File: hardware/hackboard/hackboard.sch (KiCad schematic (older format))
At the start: 22 parts, among them J1 Power, J2 Lil Cup, J3 Chonk Cup, J4 JTAG, Q1 Mosfet, Q2 Mosfet, U1 AP63200, U2 ESP32-WROVER-E

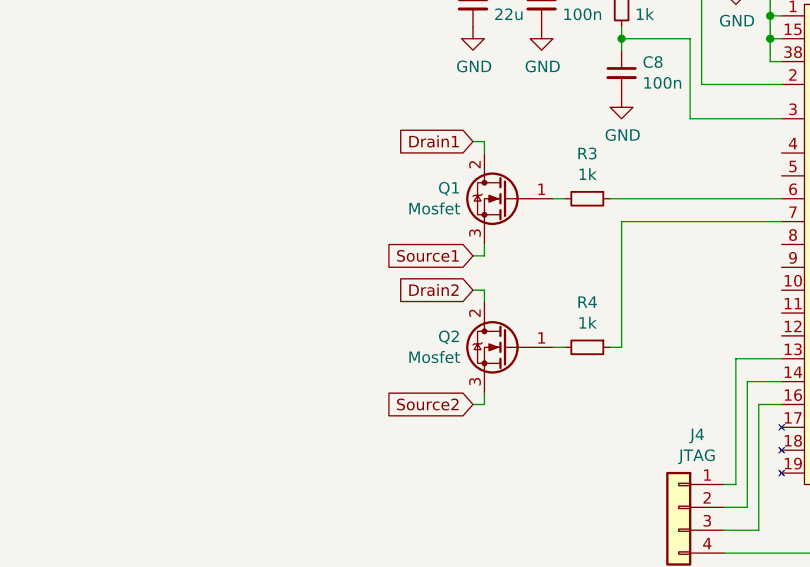
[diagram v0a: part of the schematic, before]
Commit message: Footprints zugewiesen, Bauteile angefangen zu plazieren
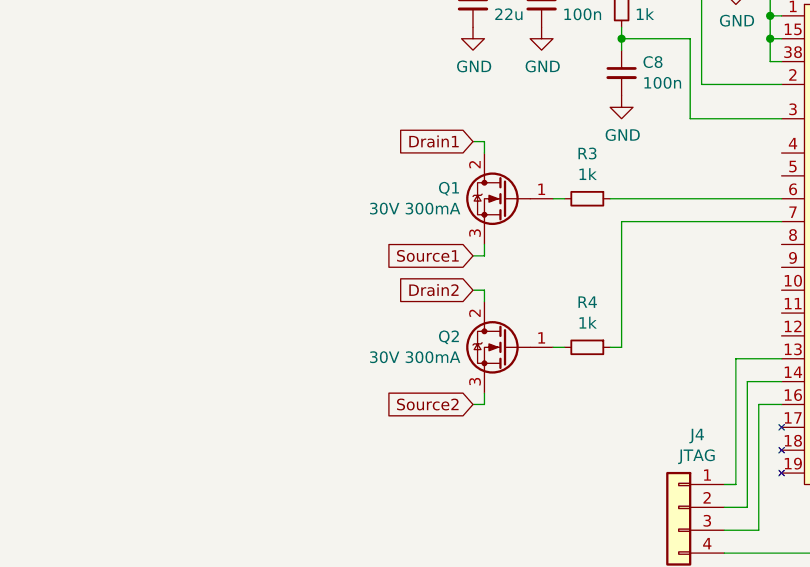
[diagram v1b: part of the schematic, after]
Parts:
- C1, C4, C5, C6: footprint (none) -> Capacitor_SMD:C_1210_3225Metric_Pad1.42x2.65mm_HandSolder
- C2, C3, C7, C8: footprint (none) -> Capacitor_SMD:C_0603_1608Metric_Pad1.05x0.95mm_HandSolder
- J1: footprint (none) -> Connector_Molex:Molex_KK-254_AE-6410-02A_1x02_P2.54mm_Vertical
- J2, J3: footprint (none) -> Connector_Molex:Molex_KK-254_AE-6410-03A_1x03_P2.54mm_Vertical
- J4: footprint (none) -> Connector_Molex:Molex_KK-254_AE-6410-06A_1x06_P2.54mm_Vertical
- L1: footprint (none) -> n-level:WE-7345
- Q1, Q2: value Mosfet -> 30V 300mA; footprint (none) -> Package_TO_SOT_SMD:SOT-23_Handsoldering
- R1, R2, R3, R4, R5: footprint (none) -> Resistor_SMD:R_0603_1608Metric_Pad1.05x0.95mm_HandSolder
- U1: footprint (none) -> Package_TO_SOT_SMD:TSOT-23-6_HandSoldering
- U2: footprint (none) -> n-level:ESP32-WROOM-ROVER
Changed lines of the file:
@@
 F 0 "U2" H 6750 2377 50  0000 C CNN
 F 1 "ESP32-WROVER-E" H 6750 2286 50  0000 C CNN
-F 2 "" H 6750 3450 50  0001 C CNN
+F 2 "n-level:ESP32-WROOM-ROVER" H 6750 3450 50  0001 C CNN
 F 3 "" H 6750 3450 50  0001 C CNN
 	1    6750 3500
@@
 F 0 "J1" H 568 2867 50  0000 C CNN
 F 1 "Power" H 568 2776 50  0000 C CNN
-F 2 "" H 650 2650 50  0001 C CNN
+F 2 "Connector_Molex:Molex_KK-254_AE-6410-02A_1x02_P2.54mm_Vertical" H 650 2650 50  0001 C CNN
 F 3 "~" H 650 2650 50  0001 C CNN
 	1    650  2650
@@
 F 0 "R1" H 3259 6846 50  0000 L CNN
 F 1 "182k" H 3259 6755 50  0000 L CNN
-F 2 "" H 3200 6800 50  0001 C CNN
+F 2 "Resistor_SMD:R_0603_1608Metric_Pad1.05x0.95mm_HandSolder" H 3200 6800 50  0001 C CNN
 F 3 "~" H 3200 6800 50  0001 C CNN
 	1    3200 6800
@@
 P 4850 3300
 F 0 "Q1" H 5055 3346 50  0000 L CNN
-F 1 "Mosfet" H 5055 3255 50  0000 L CNN
-F 2 "" H 5050 3400 50  0001 C CNN
+F 1 "30V 300mA" H 5055 3255 50  0000 L CNN
+F 2 "Package_TO_SOT_SMD:SOT-23_Handsoldering" H 5050 3400 50  0001 C CNN
 F 3 "~" H 4850 3300 50  0001 C CNN
 	1    4850 3300
@@
 F 0 "C1" H 1292 6996 50  0000 L CNN
 F 1 "10u" H 1292 6905 50  0000 L CNN
-F 2 "" H 1200 6950 50  0001 C CNN
+F 2 "Capacitor_SMD:C_1210_3225Metric_Pad1.42x2.65mm_HandSolder" H 1200 6950 50  0001 C CNN
 F 3 "~" H 1200 6950 50  0001 C CNN
 	1    1200 6950
@@
 F 0 "U1" H 1850 7415 50  0000 C CNN
 F 1 "AP63200" H 1850 7324 50  0000 C CNN
-F 2 "" H 1850 7400 50  0001 C CNN
+F 2 "Package_TO_SOT_SMD:TSOT-23-6_HandSoldering" H 1850 7400 50  0001 C CNN
 F 3 "" H 1850 7400 50  0001 C CNN
 	1    1850 6950
@@
 F 0 "C2" V 2171 6650 50  0000 C CNN
 F 1 "100n" V 2262 6650 50  0000 C CNN
-F 2 "" H 2400 6650 50  0001 C CNN
+F 2 "Capacitor_SMD:C_0603_1608Metric_Pad1.05x0.95mm_HandSolder" H 2400 6650 50  0001 C CNN
 F 3 "~" H 2400 6650 50  0001 C CNN
 	1    2400 6650
@@
 F 0 "L1" V 2885 6650 50  0000 C CNN
 F 1 "10u" V 2794 6650 50  0000 C CNN
-F 2 "" H 2700 6650 50  0001 C CNN
+F 2 "n-level:WE-7345" H 2700 6650 50  0001 C CNN
 F 3 "~" H 2700 6650 50  0001 C CNN
 	1    2700 6650
@@
 F 0 "C3" H 2942 6846 50  0000 L CNN
 F 1 "100p" H 2942 6755 50  0000 L CNN
-F 2 "" H 2850 6800 50  0001 C CNN
+F 2 "Capacitor_SMD:C_0603_1608Metric_Pad1.05x0.95mm_HandSolder" H 2850 6800 50  0001 C CNN
 F 3 "~" H 2850 6800 50  0001 C CNN
 	1    2850 6800
@@
 F 0 "R2" H 3259 7146 50  0000 L CNN
 F 1 "62k" H 3259 7055 50  0000 L CNN
-F 2 "" H 3200 7100 50  0001 C CNN
+F 2 "Resistor_SMD:R_0603_1608Metric_Pad1.05x0.95mm_HandSolder" H 3200 7100 50  0001 C CNN
 F 3 "~" H 3200 7100 50  0001 C CNN
 	1    3200 7100
@@
 F 0 "C4" H 3642 6996 50  0000 L CNN
 F 1 "22u" H 3642 6905 50  0000 L CNN
-F 2 "" H 3550 6950 50  0001 C CNN
+F 2 "Capacitor_SMD:C_1210_3225Metric_Pad1.42x2.65mm_HandSolder" H 3550 6950 50  0001 C CNN
 F 3 "~" H 3550 6950 50  0001 C CNN
 	1    3550 6950
@@
 F 0 "C5" H 3992 6996 50  0000 L CNN
 F 1 "22u" H 3992 6905 50  0000 L CNN
-F 2 "" H 3900 6950 50  0001 C CNN
+F 2 "Capacitor_SMD:C_1210_3225Metric_Pad1.42x2.65mm_HandSolder" H 3900 6950 50  0001 C CNN
 F 3 "~" H 3900 6950 50  0001 C CNN
 	1    3900 6950
@@
 F 0 "C8" H 5442 2796 50  0000 L CNN
 F 1 "100n" H 5442 2705 50  0000 L CNN
-F 2 "" H 5350 2750 50  0001 C CNN
+F 2 "Capacitor_SMD:C_0603_1608Metric_Pad1.05x0.95mm_HandSolder" H 5350 2750 50  0001 C CNN
 F 3 "~" H 5350 2750 50  0001 C CNN
 	1    5350 2750
@@
 F 0 "R5" H 5409 2496 50  0000 L CNN
 F 1 "1k" H 5409 2405 50  0000 L CNN
-F 2 "" H 5350 2450 50  0001 C CNN
+F 2 "Resistor_SMD:R_0603_1608Metric_Pad1.05x0.95mm_HandSolder" H 5350 2450 50  0001 C CNN
 F 3 "~" H 5350 2450 50  0001 C CNN
 	1    5350 2450
@@
 F 0 "C7" H 5092 2496 50  0000 L CNN
 F 1 "100n" H 5092 2405 50  0000 L CNN
-F 2 "" H 5000 2450 50  0001 C CNN
+F 2 "Capacitor_SMD:C_0603_1608Metric_Pad1.05x0.95mm_HandSolder" H 5000 2450 50  0001 C CNN
 F 3 "~" H 5000 2450 50  0001 C CNN
 	1    5000 2450
@@
 F 0 "C6" H 4792 2496 50  0000 L CNN
 F 1 "22u" H 4792 2405 50  0000 L CNN
-F 2 "" H 4700 2450 50  0001 C CNN
+F 2 "Capacitor_SMD:C_1210_3225Metric_Pad1.42x2.65mm_HandSolder" H 4700 2450 50  0001 C CNN
 F 3 "~" H 4700 2450 50  0001 C CNN
 	1    4700 2450
@@
 F 0 "J2" H 568 3717 50  0000 C CNN
 F 1 "Lil Cup" H 568 3626 50  0000 C CNN
-F 2 "" H 650 3400 50  0001 C CNN
+F 2 "Connector_Molex:Molex_KK-254_AE-6410-03A_1x03_P2.54mm_Vertical" H 650 3400 50  0001 C CNN
 F 3 "~" H 650 3400 50  0001 C CNN
 	1    650  3400
@@
 F 0 "J4" H 5518 4967 50  0000 C CNN
 F 1 "JTAG" H 5518 4876 50  0000 C CNN
-F 2 "" H 5600 4650 50  0001 C CNN
+F 2 "Connector_Molex:Molex_KK-254_AE-6410-06A_1x06_P2.54mm_Vertical" H 5600 4650 50  0001 C CNN
 F 3 "~" H 5600 4650 50  0001 C CNN
 	1    5600 4650
@@
 F 0 "J3" H 568 4467 50  0000 C CNN
 F 1 "Chonk Cup" H 568 4376 50  0000 C CNN
-F 2 "" H 650 4150 50  0001 C CNN
+F 2 "Connector_Molex:Molex_KK-254_AE-6410-03A_1x03_P2.54mm_Vertical" H 650 4150 50  0001 C CNN
 F 3 "~" H 650 4150 50  0001 C CNN
 	1    650  4150
@@
 P 4850 3950
 F 0 "Q2" H 5055 3996 50  0000 L CNN
-F 1 "Mosfet" H 5055 3905 50  0000 L CNN
-F 2 "" H 5050 4050 50  0001 C CNN
+F 1 "30V 300mA" H 5055 3905 50  0000 L CNN
+F 2 "Package_TO_SOT_SMD:SOT-23_Handsoldering" H 5050 4050 50  0001 C CNN
 F 3 "~" H 4850 3950 50  0001 C CNN
 	1    4850 3950
@@
 F 0 "R3" V 5004 3300 50  0000 C CNN
 F 1 "1k" V 5095 3300 50  0000 C CNN
-F 2 "" H 5200 3300 50  0001 C CNN
+F 2 "Resistor_SMD:R_0603_1608Metric_Pad1.05x0.95mm_HandSolder" H 5200 3300 50  0001 C CNN
 F 3 "~" H 5200 3300 50  0001 C CNN
 	1    5200 3300
@@
 F 0 "R4" V 5004 3950 50  0000 C CNN
 F 1 "1k" V 5095 3950 50  0000 C CNN
-F 2 "" H 5200 3950 50  0001 C CNN
+F 2 "Resistor_SMD:R_0603_1608Metric_Pad1.05x0.95mm_HandSolder" H 5200 3950 50  0001 C CNN
 F 3 "~" H 5200 3950 50  0001 C CNN
 	1    5200 3950

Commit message: PCB fertiggestellt
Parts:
- removed J4: JTAG, Connector_Molex:Molex_KK-254_AE-6410-06A_1x06_P2.54mm_Vertical, symbol Connector_Generic:Conn_01x04
- added J4: Programming, Connector_Molex:Molex_KK-254_AE-6410-06A_1x06_P2.54mm_Vertical, symbol Connector_Generic:Conn_01x06
- added J5: Programming Jumper, Connector_PinHeader_2.54mm:PinHeader_1x02_P2.54mm_Vertical, symbol Connector_Generic:Conn_01x02
- C3: footprint Capacitor_SMD:C_0603_1608Metric_Pad1.05x0.95mm_HandSolder -> Capacitor_SMD:C_0402_1005Metric
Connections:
- net +3V3: now also J4.5 (Pin_5)
- net GND: now also J4.6 (Pin_6), J5.2 (Pin_2)
- net Vin: now also J4.4 (Pin_4)
- net at U2.25 (IO0): now also J5.1 (Pin_1)
- net at U2.34 (RXD0): now also J4.3 (Pin_3)
- net at U2.35 (TXD0): now also J4.2 (Pin_2)
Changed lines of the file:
@@
 F 0 "C3" H 2942 6846 50  0000 L CNN
 F 1 "100p" H 2942 6755 50  0000 L CNN
-F 2 "Capacitor_SMD:C_0603_1608Metric_Pad1.05x0.95mm_HandSolder" H 2850 6800 50  0001 C CNN
+F 2 "Capacitor_SMD:C_0402_1005Metric" H 2850 6800 50  0001 C CNN
 F 3 "~" H 2850 6800 50  0001 C CNN
 	1    2850 6800
@@
 	-1   0    0    -1
 $EndComp
-$Comp
-L Connector_Generic:Conn_01x04 J4
-U 1 1 6237B1F1
-P 5600 4650
-F 0 "J4" H 5518 4967 50  0000 C CNN
-F 1 "JTAG" H 5518 4876 50  0000 C CNN
-F 2 "Connector_Molex:Molex_KK-254_AE-6410-06A_1x06_P2.54mm_Vertical" H 5600 4650 50  0001 C CNN
-F 3 "~" H 5600 4650 50  0001 C CNN
-	1    5600 4650
-	-1   0    0    -1
-$EndComp
-Wire Wire Line
-	6050 4200 5950 4200
-Wire Wire Line
-	5950 4200 5950 4750
-Wire Wire Line
-	6050 4100 5900 4100
-Wire Wire Line
-	5900 4100 5900 4650
-Wire Wire Line
-	6050 4000 5850 4000
-Wire Wire Line
-	5850 4000 5850 4550
-Wire Wire Line
-	5850 4550 5800 4550
-Wire Wire Line
-	5800 4650 5900 4650
-Wire Wire Line
-	5800 4750 5950 4750
-Wire Wire Line
-	5800 4850 7550 4850
-Wire Wire Line
-	7550 4850 7550 3600
-Wire Wire Line
-	7550 3600 7450 3600
 Wire Wire Line
 	5850 2300 6000 2300
@@
 Wire Wire Line
 	5350 3400 6050 3400
+$Comp
+L Connector_Generic:Conn_01x06 J4
+U 1 1 623EC92C
+P 8550 2800
+F 0 "J4" H 8630 2792 50  0000 L CNN
+F 1 "Programming" H 8630 2701 50  0000 L CNN
+F 2 "Connector_Molex:Molex_KK-254_AE-6410-06A_1x06_P2.54mm_Vertical" H 8550 2800 50  0001 C CNN
+F 3 "~" H 8550 2800 50  0001 C CNN
+	1    8550 2800
+	1    0    0    -1
+$EndComp
+$Comp
+L power:+3V3 #PWR0101
+U 1 1 623FC433
+P 7950 3050
+F 0 "#PWR0101" H 7950 2900 50  0001 C CNN
+F 1 "+3V3" H 7965 3223 50  0000 C CNN
+F 2 "" H 7950 3050 50  0001 C CNN
+F 3 "" H 7950 3050 50  0001 C CNN
+	1    7950 3050
+	1    0    0    -1
+$EndComp
+Wire Wire Line
+	7450 2800 8350 2800
+Wire Wire Line
+	7450 2700 8350 2700
+Text GLabel 8300 2900 0    50   Input ~ 0
+Vin
+Wire Wire Line
+	7950 3100 7950 3050
+Wire Wire Line
+	8300 2900 8350 2900
+$Comp
+L power:GND #PWR0102
+U 1 1 6241482D
+P 8300 3150
+F 0 "#PWR0102" H 8300 2900 50  0001 C CNN
+F 1 "GND" H 8305 2977 50  0000 C CNN
+F 2 "" H 8300 3150 50  0001 C CNN
+F 3 "" H 8300 3150 50  0001 C CNN
+	1    8300 3150
+	1    0    0    -1
+$EndComp
+Wire Wire Line
+	8300 3150 8300 3100
+Wire Wire Line
+	8300 3100 8350 3100
+Wire Wire Line
+	7950 3100 8150 3100
+Wire Wire Line
+	8150 3100 8150 3000
+Wire Wire Line
+	8150 3000 8350 3000
+$Comp
+L Connector_Generic:Conn_01x02 J5
+U 1 1 6242E468
+P 8550 3450
+F 0 "J5" H 8630 3442 50  0000 L CNN
+F 1 "Programming Jumper" H 8630 3351 50  0000 L CNN
+F 2 "Connector_PinHeader_2.54mm:PinHeader_1x02_P2.54mm_Vertical" H 8550 3450 50  0001 C CNN
+F 3 "~" H 8550 3450 50  0001 C CNN
+	1    8550 3450
+	1    0    0    -1
+$EndComp
+Wire Wire Line
+	8150 3400 8150 3450
+Wire Wire Line
+	8150 3450 8350 3450
+Wire Wire Line
+	7450 3400 8150 3400
+$Comp
+L power:GND #PWR0103
+U 1 1 62433817
+P 8300 3600
+F 0 "#PWR0103" H 8300 3350 50  0001 C CNN
+F 1 "GND" H 8305 3427 50  0000 C CNN
+F 2 "" H 8300 3600 50  0001 C CNN
+F 3 "" H 8300 3600 50  0001 C CNN
+	1    8300 3600
+	1    0    0    -1
+$EndComp
+Wire Wire Line
+	8300 3600 8300 3550
+Wire Wire Line
+	8300 3550 8350 3550
 $EndSCHEMATC
